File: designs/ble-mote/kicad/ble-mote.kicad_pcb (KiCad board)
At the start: 4 copper layers, 35 x 25 mm, 37 parts

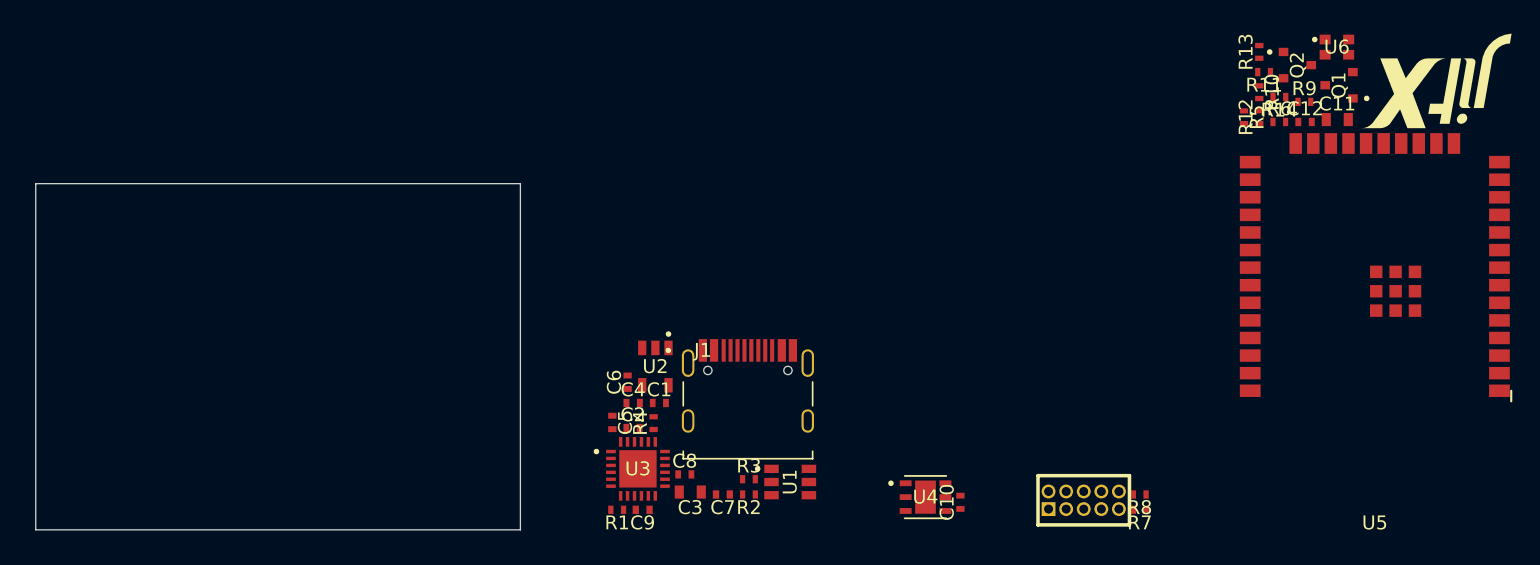
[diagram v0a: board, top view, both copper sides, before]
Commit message: Schematic export issue in kicad
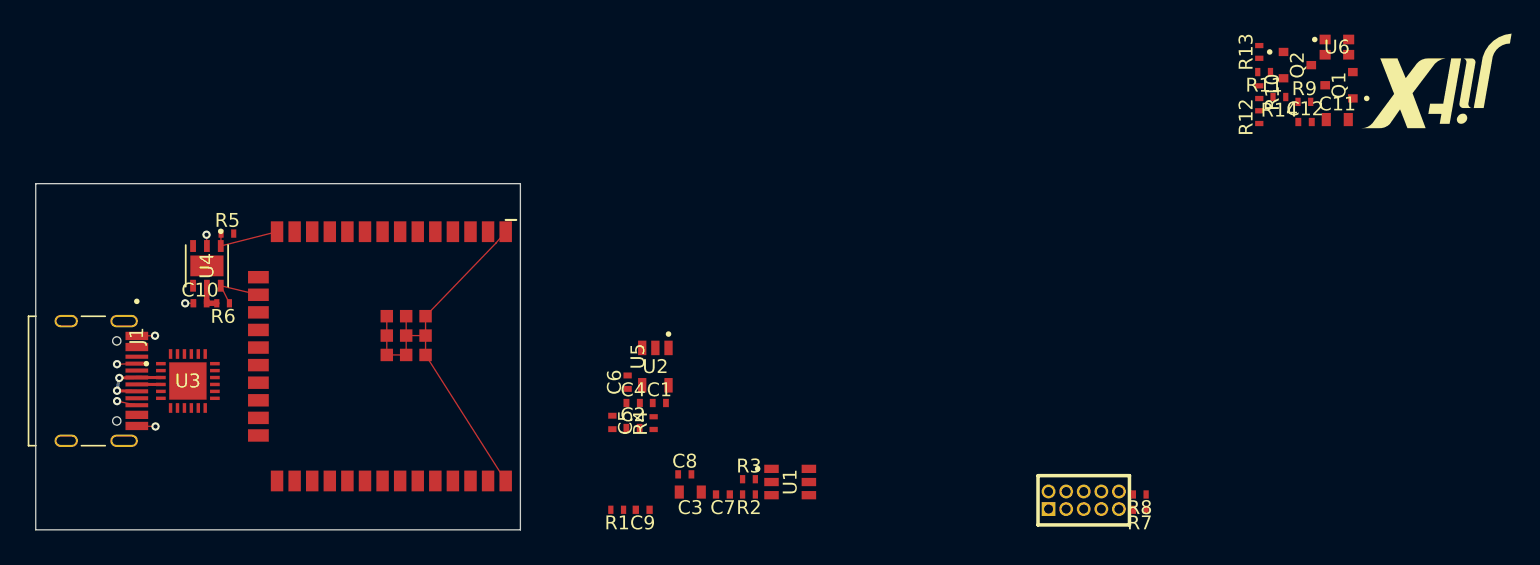
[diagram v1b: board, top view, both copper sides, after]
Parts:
- moved R6 77.4 mm to (135.5, 104.1), turned to 270 degrees
- moved R5 73.9 mm to (135.8, 99.1), turned to 90 degrees
- moved U5 67.9 mm to (150.8, 108.0), turned to 270 degrees
- moved C10 56.8 mm to (133.9, 104.1), turned to 90 degrees
- moved U4 54.5 mm to (134.4, 101.4), turned to 270 degrees
- moved J1 40.9 mm to (129.3, 106.5), turned to 270 degrees
- moved U3 33.1 mm to (133.0, 109.8)
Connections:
- net usb_rid_rid_p1 renamed cap_p1
- Q1 pad 1: proc_q0_b -> b
- R10 pad 2: proc_q0_b -> b
- R14 pad 2: b -> l_b
- U5 pad 10: H-I2C_scl -> pc-uart_rx
- U5 pad 11: H-I2C_sda -> control-pins2_timer
- U5 pad 14: (no net) -> H-I2C_sda
- U5 pad 16: (no net) -> H-I2C_scl
- U5 pad 23: pc-ctrl0_gpio -> (no net)
- U5 pad 30: control-pins0_timer -> (no net)
- U5 pad 31: pc-ctrl1_gpio -> pc-ctrl0_gpio
- U5 pad 33: pc-uart_tx -> control-pins0_timer
- U5 pad 36: pc-uart_rx -> pc-ctrl1_gpio
- U5 pad 37: control-pins2_timer -> pc-uart_tx
- U6 pad 2: b -> l_b
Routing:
- net gnd: track 0.00 -> 34.5 mm, vias 0 -> 4
- net D+: track 0.00 -> 5.37 mm, vias 0 -> 2
- net H-I2C_sda: track 0.00 -> 5.09 mm
- net H-I2C_scl: track 0.00 -> 4.21 mm
- net P3V3: track 0.00 -> 2.00 mm
- net D-: track 0.00 -> 1.74 mm
- net rid_p1: track 0.00 -> 1.45 mm, vias 0 -> 1
- net rid_rid_p1: track 0.00 -> 1.43 mm, vias 0 -> 1
